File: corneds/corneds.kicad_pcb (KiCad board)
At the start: 2 copper layers, 118 parts, among them J1 Conn_ARM_SWD_TagConnect_TC203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, J2 Conn_ARM_SWD_TagConnect_TC203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, J3 AudioJack4, J4 AudioJack4, SW1 SW_Push, SW10 SW_Push, SW11 SW_Push, SW12 SW_Push, SW13 SW_Push, SW14 SW_Push, SW15 SW_Push, SW16 SW_Push, SW17 SW_Push, SW18 SW_Push, SW19 SW_Push, SW2 SW_Push, SW20 SW_Push, SW21 SW_Push, SW22 SW_Push, SW23 SW_Push, SW24 SW_Push, SW25 SW_Push, SW26 SW_Push, SW27 SW_Push, SW28 SW_Push, SW29 SW_Push, SW3 SW_Push, SW30 SW_Push, SW31 SW_Push, SW32 SW_Push, SW33 SW_Push, SW34 SW_Push, SW35 SW_Push, SW36 SW_Push, SW37 SW_Push, SW38 SW_Push, SW39 SW_Push, SW4 SW_Push, SW40 SW_Push, SW41 SW_Push, SW42 SW_Push, SW5 SW_Push, SW6 SW_Push, SW7 SW_Push, SW8 SW_Push, SW9 SW_Push, U1 Pico, U2 Pico

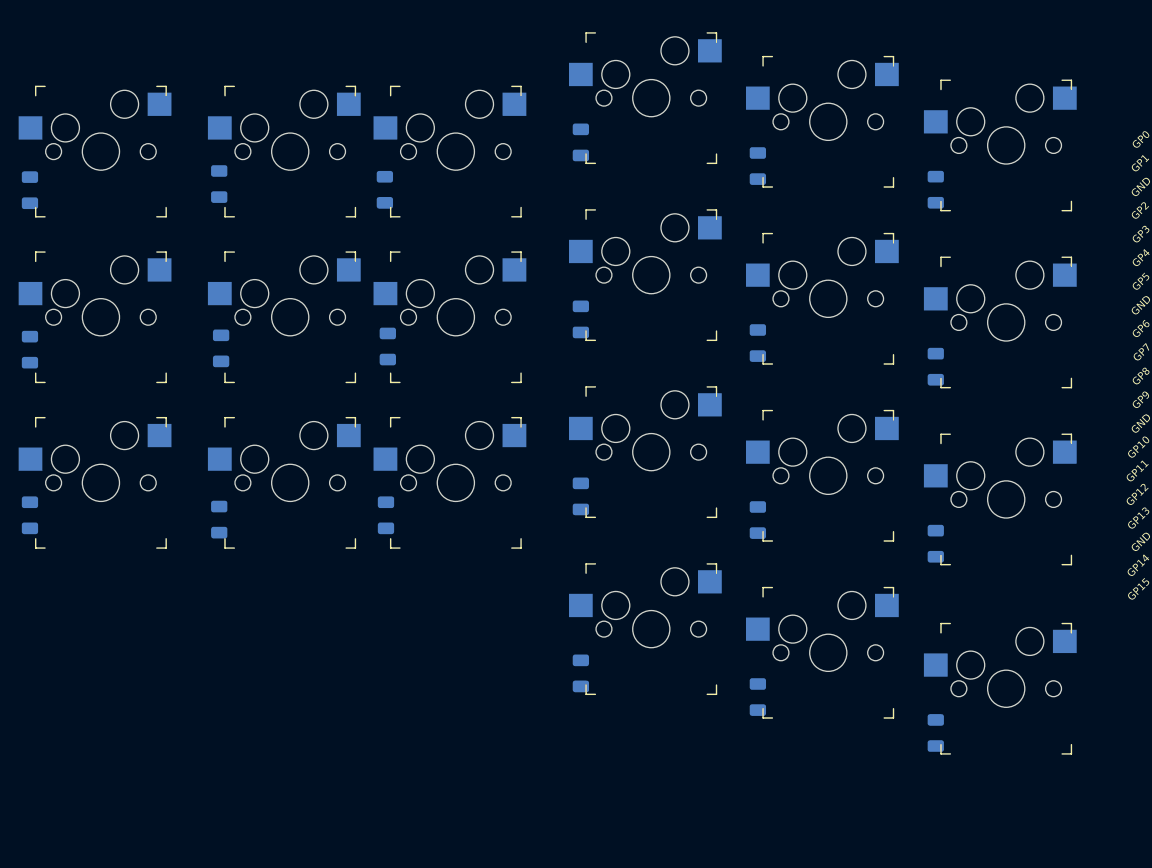
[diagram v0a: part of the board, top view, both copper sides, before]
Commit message: no longer committing backups and left side of keyboard almost done placement
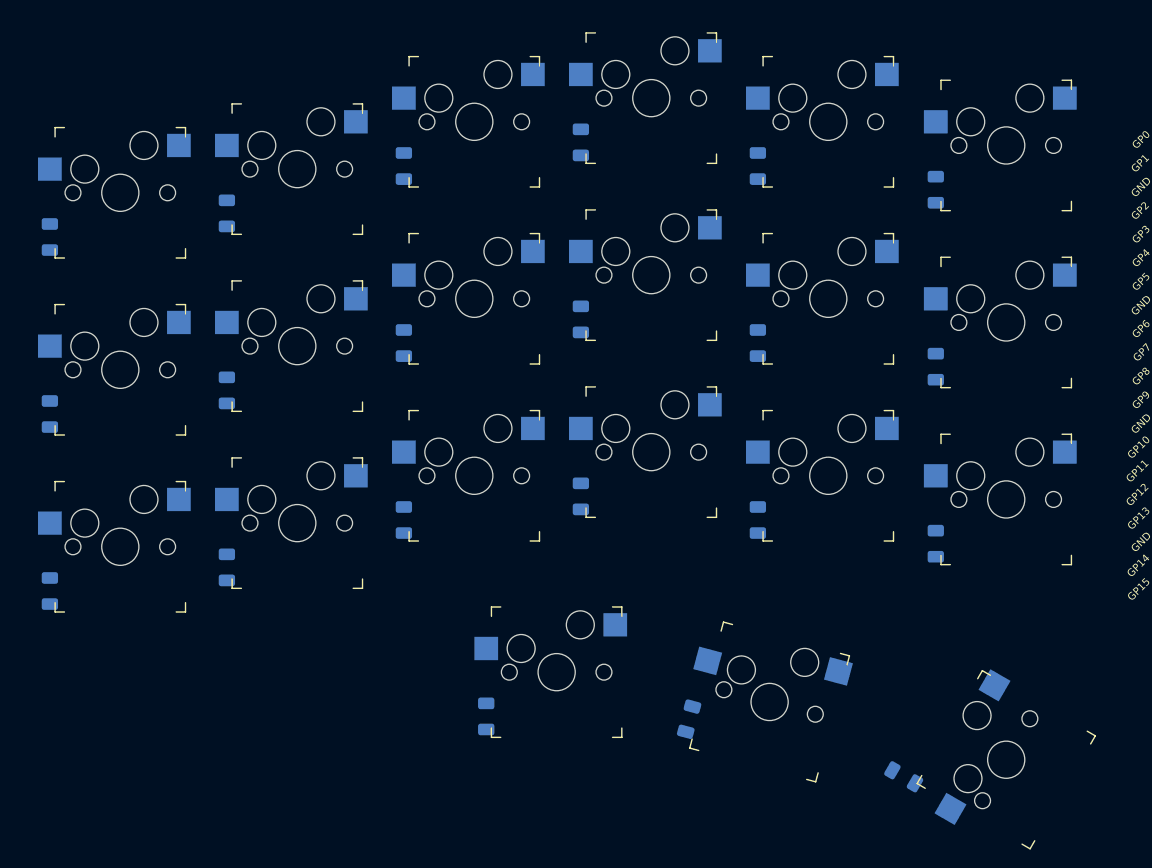
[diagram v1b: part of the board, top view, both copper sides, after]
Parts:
- moved D22 11.2 mm to (36.3, 108.9)
- moved SW22 11.2 mm to (43.8, 104.1)
- moved D3 8.41 mm to (-10.6, 95.4)
- moved SW30 8.22 mm to (66.7, 107.3), turned to -15 degrees
- moved D30 7.76 mm to (58.1, 109.2), turned to 75 degrees
- moved SW38 7.62 mm to (92.1, 113.5), turned to 60 degrees
- moved D2 7.23 mm to (-10.6, 76.4)
- moved SW3 7.17 mm to (-3.00, 90.7)
- moved SW2 6.01 mm to (-3.00, 71.7)
- moved D38 5.83 mm to (81.1, 115.4), turned to -30 degrees
- moved D1 5.47 mm to (-10.6, 57.4)
- moved D9 5.20 mm to (8.44, 92.9)
- moved SW1 4.88 mm to (-3.00, 52.7)
- moved D8 4.55 mm to (8.44, 73.9)
- moved SW9 4.39 mm to (16.0, 88.1)
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
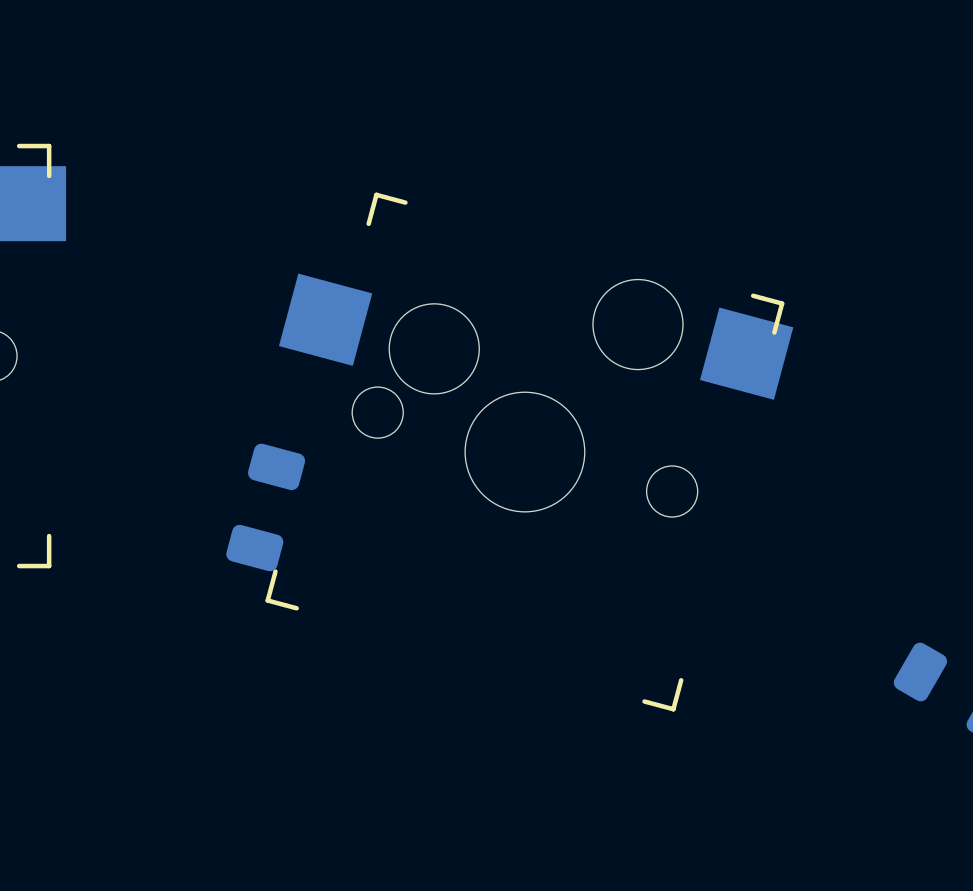
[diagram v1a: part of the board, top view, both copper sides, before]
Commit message: finished left mod key
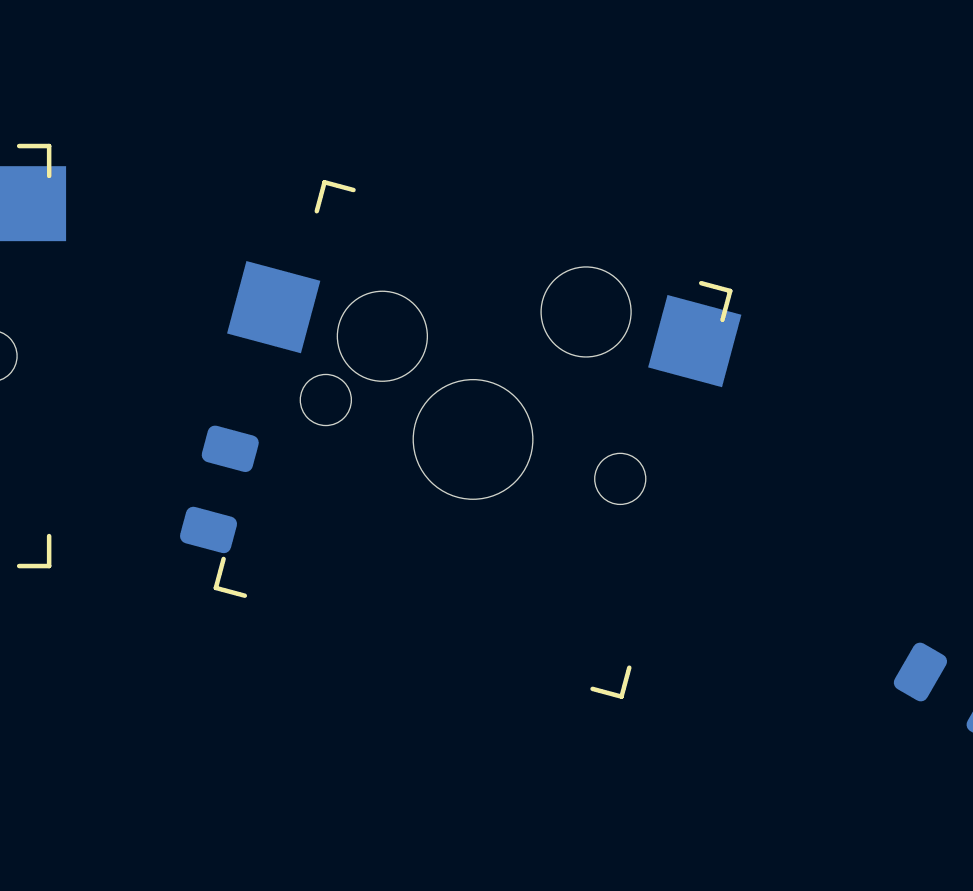
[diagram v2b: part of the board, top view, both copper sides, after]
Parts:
- moved SW30 1.78 mm to (65.0, 106.9)
- moved D30 1.66 mm to (56.5, 108.6)
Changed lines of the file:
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@@
   )
   (footprint "Key_Switches:Kailh_socket_MX" (layer "F.Cu")
-    (at 66.7 107.34 -15)
+    (at 64.97 106.92 -15)
     (descr "MX-style keyswitch with Kailh socket mount")
     (tags "MX,cherry,gateron,kailh,pg1511,socket")
@@
   )
   (footprint "Diode_SMD:D_1206_3216Metric" (layer "B.Cu")
-    (at 58.058163 109.187704 75)
+    (at 56.515 108.585 75)
     (descr "Diode SMD 1206 (3216 Metric), square (rectangular) end terminal, IPC_7351 nominal, (Body size source: http://www.tortai-tech.com/upload/download/2011102023233369053.pdf), generated with kicad-footprint-generator")
     (tags "diode")

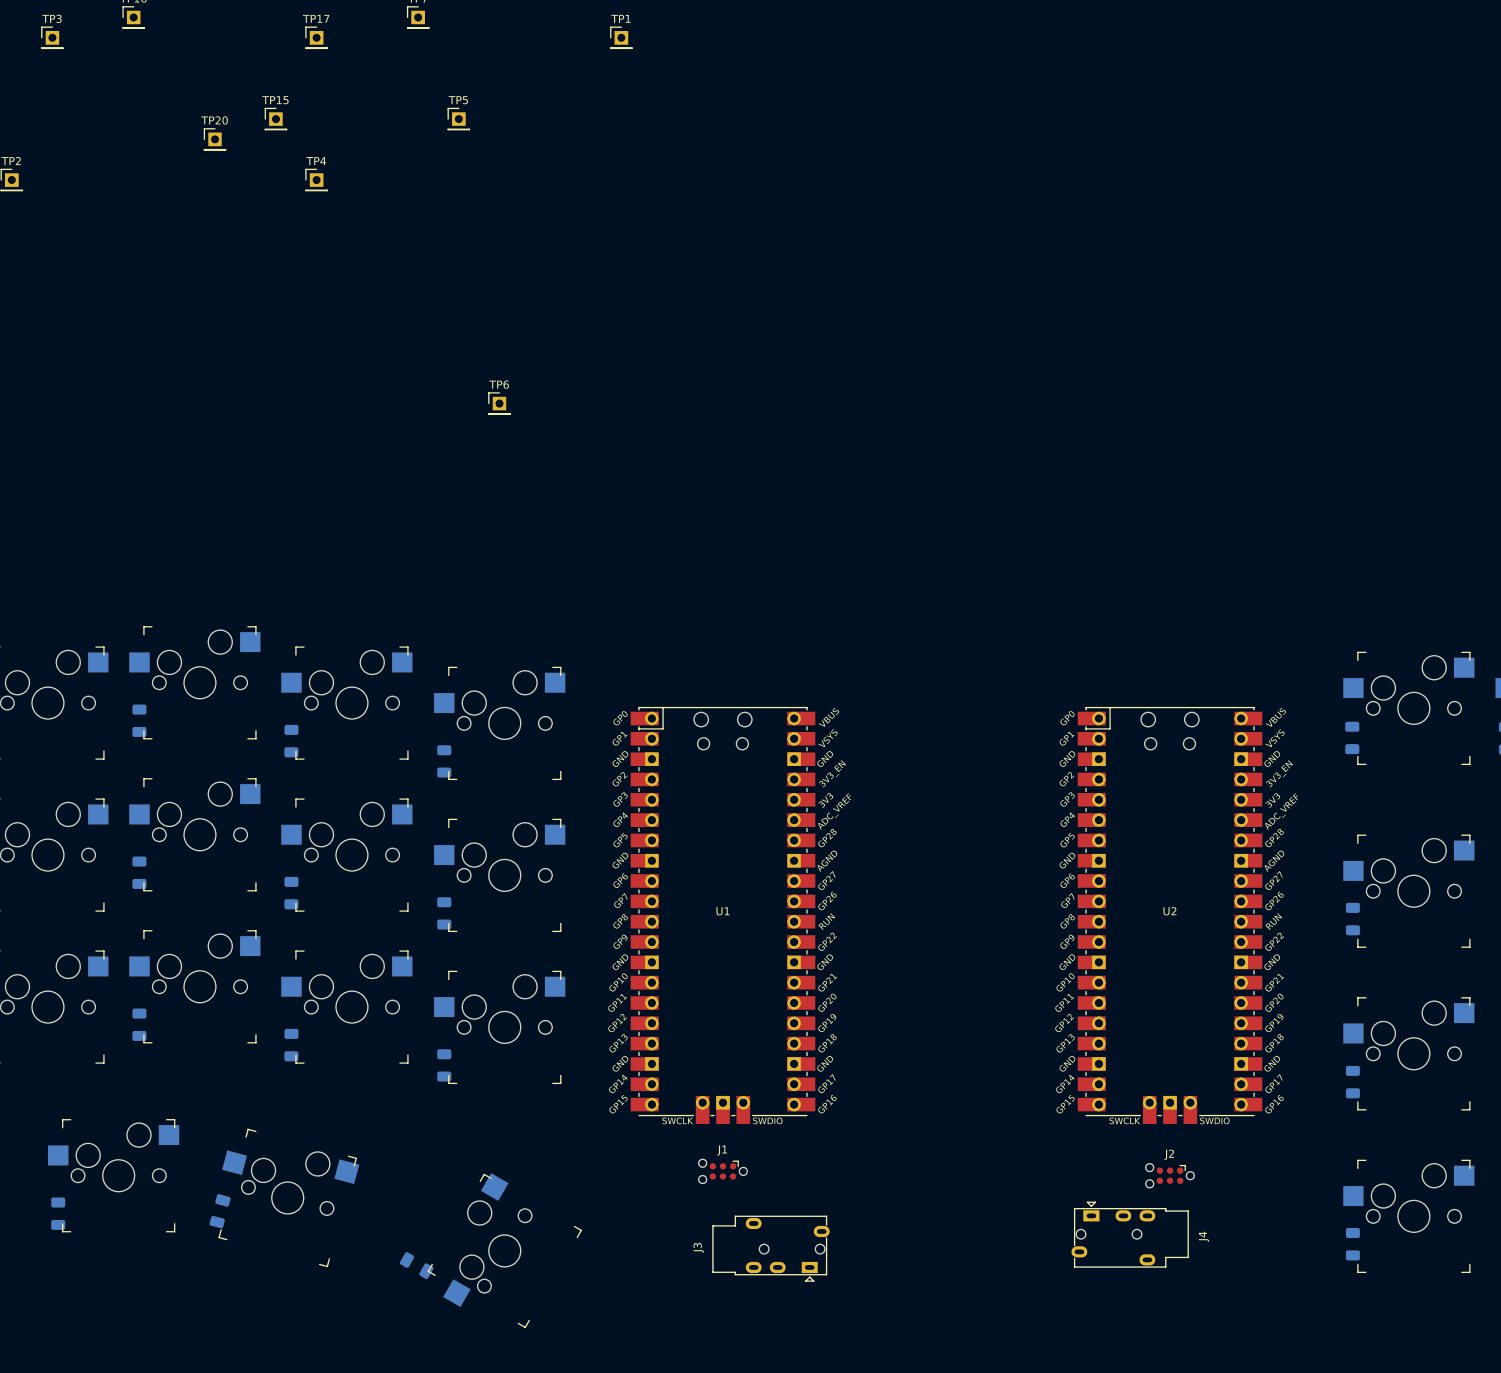
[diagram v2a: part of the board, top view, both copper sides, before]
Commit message: finished placing left side
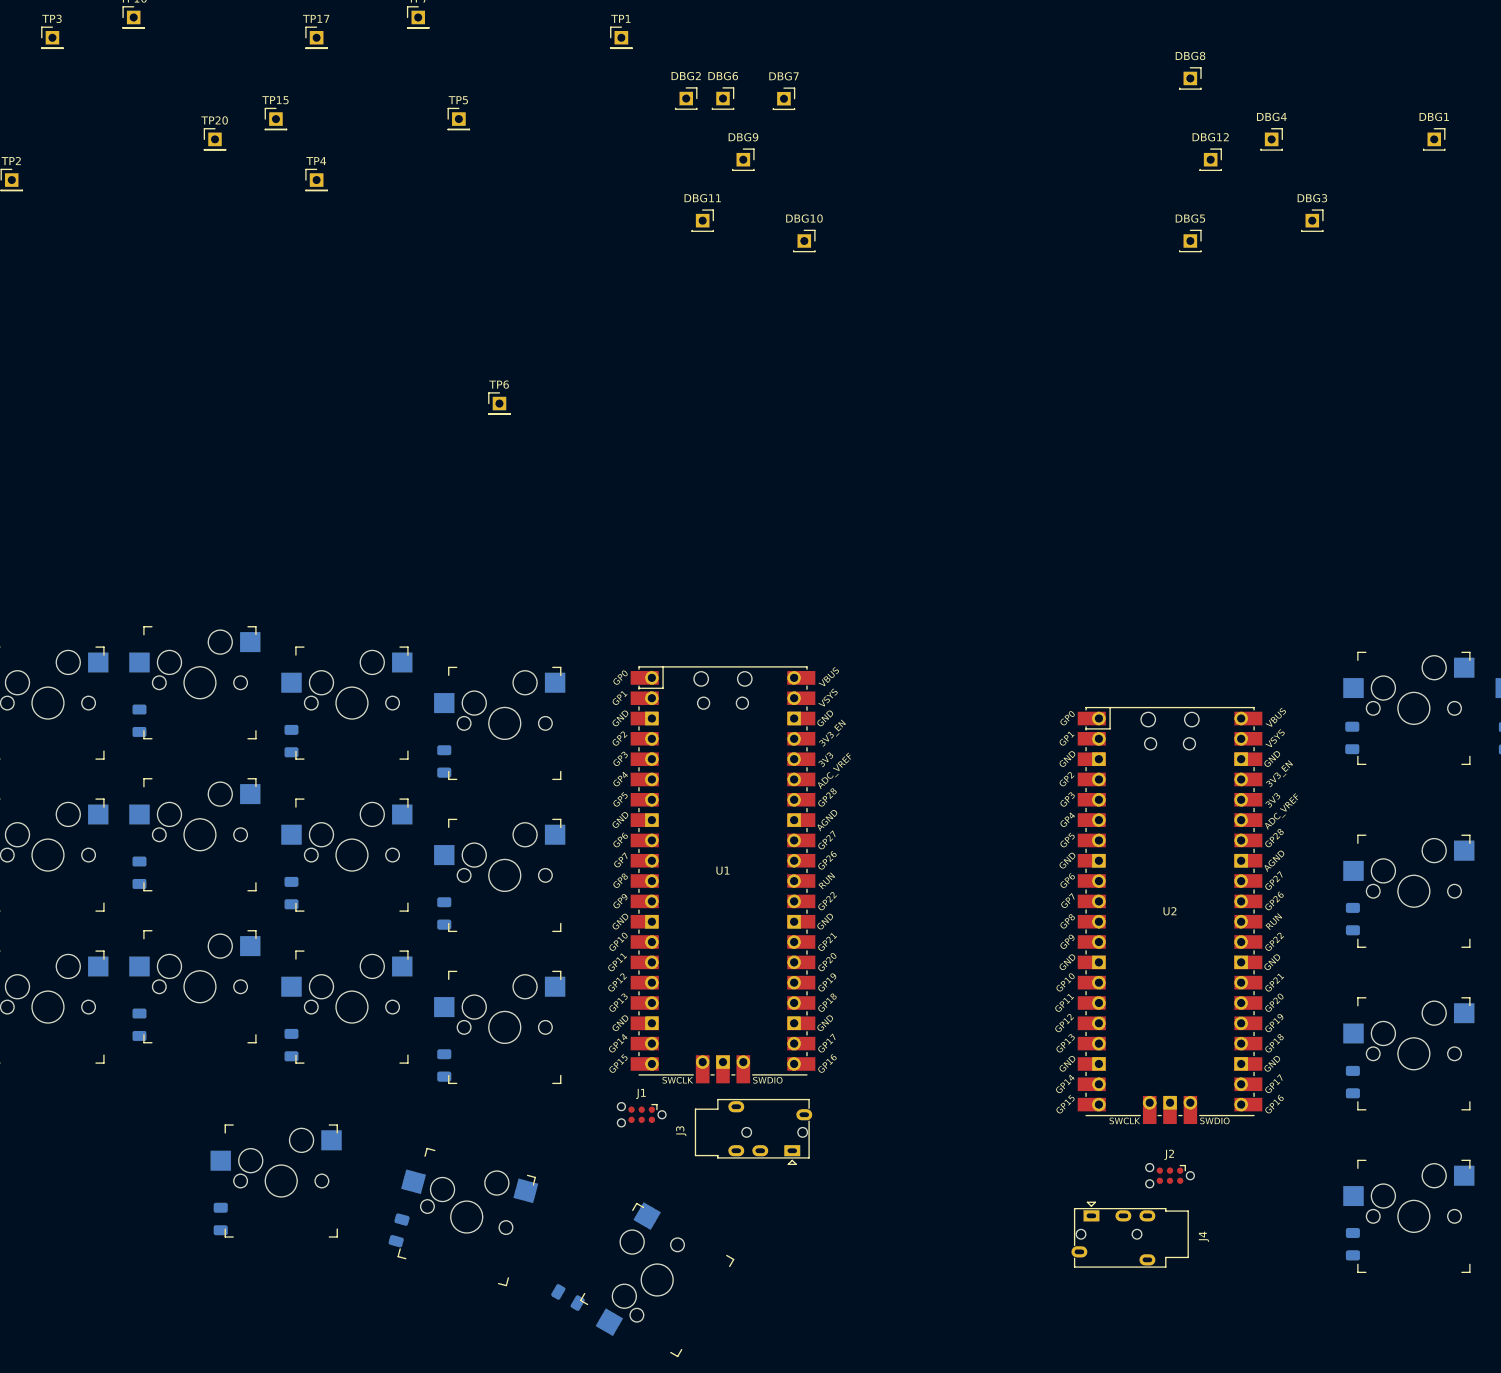
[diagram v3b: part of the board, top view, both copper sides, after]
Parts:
- added DBG1: GND, Connector_PinSocket_2.54mm:PinSocket_1x01_P2.54mm_Vertical, F.Cu at (208.3, -25.4)
- added DBG10: TX, Connector_PinSocket_2.54mm:PinSocket_1x01_P2.54mm_Vertical, F.Cu at (129.5, -12.7)
- added DBG11: RX, Connector_PinSocket_2.54mm:PinSocket_1x01_P2.54mm_Vertical, F.Cu at (116.8, -15.2)
- added DBG12: RTS, Connector_PinSocket_2.54mm:PinSocket_1x01_P2.54mm_Vertical, F.Cu at (180.3, -22.9)
- added DBG2: CTS, Connector_PinSocket_2.54mm:PinSocket_1x01_P2.54mm_Vertical, F.Cu at (114.8, -30.5)
- added DBG3: 5V, Connector_PinSocket_2.54mm:PinSocket_1x01_P2.54mm_Vertical, F.Cu at (193.0, -15.2)
- added DBG4: TX, Connector_PinSocket_2.54mm:PinSocket_1x01_P2.54mm_Vertical, F.Cu at (188.0, -25.4)
- added DBG5: RX, Connector_PinSocket_2.54mm:PinSocket_1x01_P2.54mm_Vertical, F.Cu at (177.8, -12.7)
- added DBG6: RTS, Connector_PinSocket_2.54mm:PinSocket_1x01_P2.54mm_Vertical, F.Cu at (119.4, -30.5)
- added DBG7: GND, Connector_PinSocket_2.54mm:PinSocket_1x01_P2.54mm_Vertical, F.Cu at (127.0, -30.5)
- added DBG8: CTS, Connector_PinSocket_2.54mm:PinSocket_1x01_P2.54mm_Vertical, F.Cu at (177.8, -33.0)
- added DBG9: 5V, Connector_PinSocket_2.54mm:PinSocket_1x01_P2.54mm_Vertical, F.Cu at (121.9, -22.9)
- moved D30 22.5 mm to (78.9, 111.0)
- moved SW30 22.5 mm to (87.3, 109.3)
- moved D22 20.3 mm to (56.6, 109.5)
- moved SW22 20.3 mm to (64.2, 104.8)
- moved SW38 19.4 mm to (111.2, 117.2)
- moved D38 19.3 mm to (100.0, 119.4)
- moved J3 14.8 mm to (128.0, 101.0)
- moved J1 12.4 mm to (109.2, 96.5)
- moved U1 5.08 mm to (119.4, 66.0)
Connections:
- J1 pad 3: /dbg_uart_tx_l -> unconnected-(J1-Pad3)
- J1 pad 6: /dbg_uart_rx_l -> unconnected-(J1-Pad6)
- J2 pad 3: /dbg_uart_tx_r -> unconnected-(J2-Pad3)
- J2 pad 6: /dbg_uart_rx_r -> unconnected-(J2-Pad6)

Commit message: working on routing
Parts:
- moved DBG6 186.0 mm to (-8.89, 104.1)
- moved DBG7 182.5 mm to (3.81, 104.1)
- moved DBG8 179.4 mm to (293.5, 104.1), turned to 180 degrees
- moved DBG2 177.8 mm to (-1.27, 104.1)
- moved DBG10 177.3 mm to (-3.81, 104.1)
- moved DBG9 175.2 mm to (1.27, 104.1)
- moved GP1 173.0 mm to (7.62, 104.1)
- moved DBG11 171.5 mm to (-6.35, 104.1)
- moved TP1 170.5 mm to (12.7, 104.1)
- moved DBG4 165.5 mm to (290.9, 104.1), turned to 180 degrees
- moved DBG12 165.1 mm to (285.9, 104.1), turned to 180 degrees
- moved TP19 162.6 mm to (38.1, 104.1)
- moved TP24 161.2 mm to (256.9, 104.1)
- moved DBG5 160.9 mm to (288.4, 104.1), turned to 180 degrees
- moved DBG1 157.9 mm to (298.6, 104.1), turned to 180 degrees
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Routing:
- net /col0_r: track 0.00 -> 224.9 mm
- net /vcc_l: track 0.00 -> 223.3 mm
- net /col1_r: track 0.00 -> 204.1 mm, vias 0 -> 3
- net /col3_r: track 0.00 -> 202.2 mm, vias 0 -> 5
- net /col4_r: track 0.00 -> 199.6 mm, vias 0 -> 5
- net /col5_r: track 0.00 -> 199.3 mm, vias 0 -> 4
- net /col0_l: track 0.00 -> 188.2 mm, vias 0 -> 4
- net /row1_l: track 0.00 -> 181.2 mm, vias 0 -> 2
- net /col2_r: track 0.00 -> 179.2 mm, vias 0 -> 3
- net /dbg_uart_tx_l: track 0.00 -> 177.1 mm, vias 0 -> 1
- net /row0_l: track 0.00 -> 175.9 mm, vias 0 -> 2
- net /row0_r: track 0.00 -> 173.4 mm, vias 0 -> 1
- net /row2_r: track 0.00 -> 173.2 mm, vias 0 -> 2
- net /dbg_uart_rx_l: track 0.00 -> 171.0 mm, vias 0 -> 1
- net /row1_r: track 0.00 -> 170.9 mm, vias 0 -> 3
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- added copper zone on F.Cu, net (none)
- added copper zone on B.Cu, net /gnd_l
- added copper zone on F.Cu, net /gnd_l
- added copper zone on B.Cu, net /gnd_r
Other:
- board outline added: 320 x 104.9 mm
